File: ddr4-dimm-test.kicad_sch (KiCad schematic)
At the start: 1 part

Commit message: Update readme lol
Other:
- company: (none) -> WifiCable
- title: (none) -> Wifi-DDR4-UDIMM
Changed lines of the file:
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@@
 	(generator_version "8.0")
 	(paper "A2")
+	(title_block
+		(title "Wifi-DDR4-UDIMM")
+		(company "WifiCable")
+	)
 	(junction
 		(at 74.93 269.24)

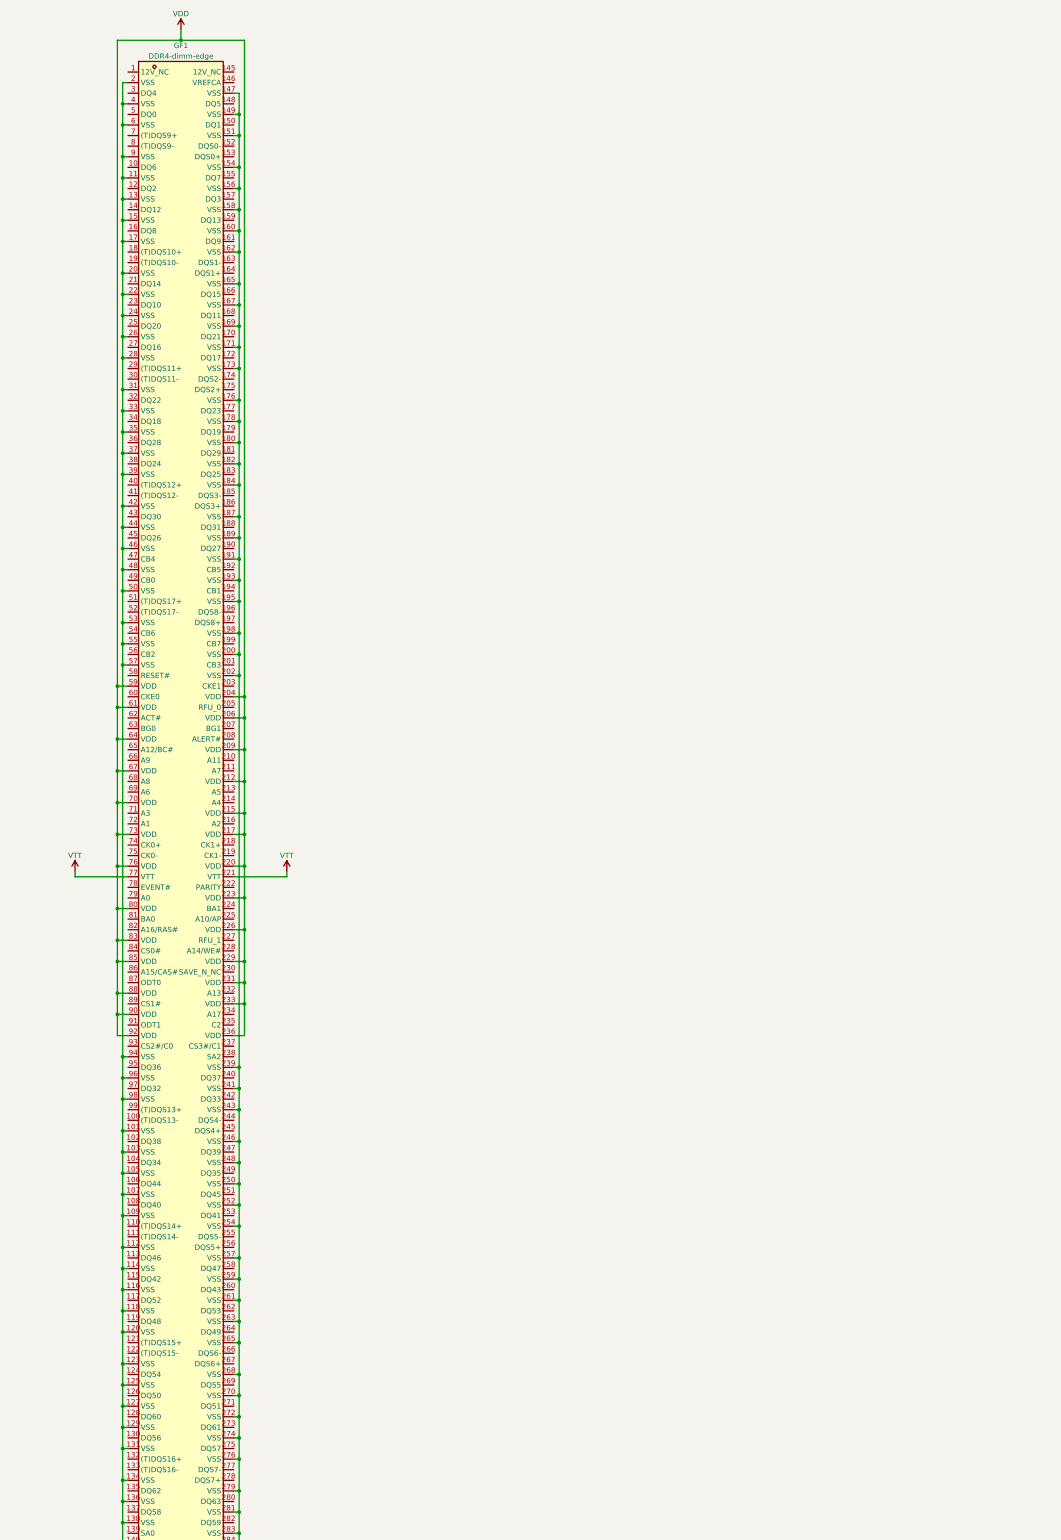
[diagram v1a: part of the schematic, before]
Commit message: Added ram chip symbol and partial connections
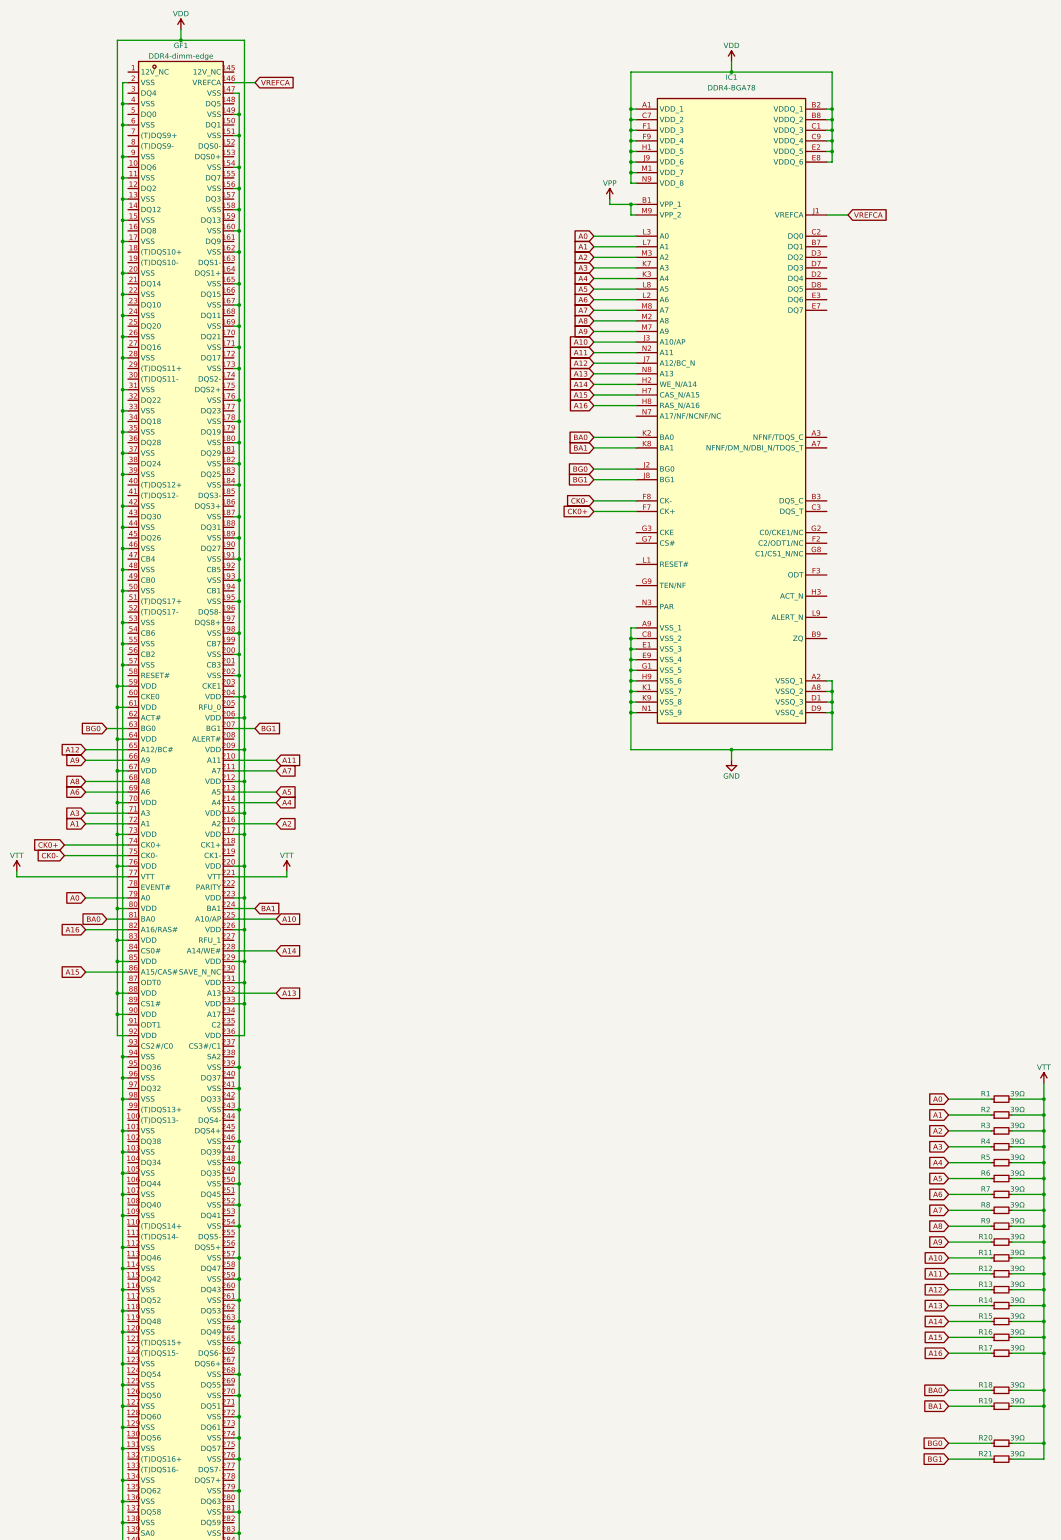
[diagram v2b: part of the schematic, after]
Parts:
- added IC1: DDR4-BGA78, A_my_stuff:DDR4-BGA78, symbol A_my_stuff:DDR4-BGA78
- added R1, R10, R11, R12, R13, R14, R15, R16, R17, R18, R19, R2, R20, R21, R3, R4, R5, R6, R7, R8, R9: 39Ω, Resistor_SMD:R_0402_1005Metric, symbol Device:R_Small
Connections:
- net GND: now also IC1.A2 (VSSQ_1), IC1.A8 (VSSQ_2), IC1.A9 (VSS_1), IC1.C8 (VSS_2), IC1.D1 (VSSQ_3), IC1.D9 (VSSQ_4), IC1.E1 (VSS_3), IC1.E9 (VSS_4), IC1.G1 (VSS_5), IC1.H9 (VSS_6), IC1.K1 (VSS_7), IC1.K9 (VSS_8), IC1.N1 (VSS_9)
- net VDD: now also IC1.A1 (VDD_1), IC1.B2 (VDDQ_1), IC1.B8 (VDDQ_2), IC1.C1 (VDDQ_3), IC1.C7 (VDD_2), IC1.C9 (VDDQ_4), IC1.E2 (VDDQ_5), IC1.E8 (VDDQ_6), IC1.F1 (VDD_3), IC1.F9 (VDD_4), IC1.H1 (VDD_5), IC1.J9 (VDD_6), IC1.M1 (VDD_7), IC1.N9 (VDD_8)
- net VPP: now also IC1.B1 (VPP_1), IC1.M9 (VPP_2)
- net VTT: now also R1.2, R10.2, R11.2, R12.2, R13.2, R14.2, R15.2, R16.2, R17.2, R18.2, R19.2, R2.2, R20.2, R21.2, R3.2, R4.2, R5.2, R6.2, R7.2, R8.2, R9.2
- net VREFCA: now reaches GF1.146 (VREFCA)
- net VREFCA: now also IC1.J1 (VREFCA)
- net BG1: now reaches GF1.207 (BG1)
- net BG1: now also IC1.J8 (BG1), R21.1
- net A11: now reaches GF1.210 (A11)
- net A11: now also IC1.N2 (A11), R12.1
- net A7: now reaches GF1.211 (A7)
- net A7: now also IC1.M8 (A7), R8.1
- net A5: now reaches GF1.213 (A5)
- net A5: now also IC1.L8 (A5), R6.1
- net A4: now reaches GF1.214 (A4)
- net A4: now also IC1.K3 (A4), R5.1
- net A2: now reaches GF1.216 (A2)
- net A2: now also IC1.M3 (A2), R3.1
- net BA1: now reaches GF1.224 (BA1)
- net BA1: now also IC1.K8 (BA1), R19.1
- net A10: now reaches GF1.225 (A10/AP)
- net A10: now also IC1.J3 (A10/AP), R11.1
- net A14: now reaches GF1.228 (A14/WE#)
- net A14: now also IC1.H2 (WE_N/A14), R15.1
- net A13: now reaches GF1.232 (A13)
- net A13: now also IC1.N8 (A13), R14.1
- net BG0: now reaches GF1.63 (BG0)
- net BG0: now also IC1.J2 (BG0), R20.1
- net A12: now reaches GF1.65 (A12/BC#)
- net A12: now also IC1.J7 (A12/BC_N), R13.1
- net A9: now reaches GF1.66 (A9)
- net A9: now also IC1.M7 (A9), R10.1
- net A8: now reaches GF1.68 (A8)
- net A8: now also IC1.M2 (A8), R9.1
- net A6: now reaches GF1.69 (A6)
- net A6: now also IC1.L2 (A6), R7.1
- net A3: now reaches GF1.71 (A3)
- net A3: now also IC1.K7 (A3), R4.1
- net A1: now reaches GF1.72 (A1)
- net A1: now also IC1.L7 (A1), R2.1
- net CK0+: now reaches GF1.74 (CK0+)
- net CK0+: now also IC1.F7 (CK+)
- net CK0-: now reaches GF1.75 (CK0-)
- net CK0-: now also IC1.F8 (CK-)
- net A0: now reaches GF1.79 (A0)
- net A0: now also IC1.L3 (A0), R1.1
- net BA0: now reaches GF1.81 (BA0)
- net BA0: now also IC1.K2 (BA0), R18.1
- net A16: now reaches GF1.82 (A16/RAS#)
- net A16: now also IC1.H8 (RAS_N/A16), R17.1
- net A15: now reaches GF1.86 (A15/CAS#)
- net A15: now also IC1.H7 (CAS_N/A15), R16.1

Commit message: Connected all common lines and duplicated chip
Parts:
- added C1: 0.01uF, Capacitor_SMD:C_0402_1005Metric, symbol Device:C_Small
- added C2: ?, Capacitor_SMD:C_0402_1005Metric, symbol Device:C_Small
- added C3: 10pF, Capacitor_SMD:C_0402_1005Metric, symbol Device:C_Small
- added IC2, IC3, IC4, IC5, IC6, IC7, IC8: DDR4-BGA78, A_my_stuff:DDR4-BGA78, symbol A_my_stuff:DDR4-BGA78
- added R22, R23, R24, R25, R26, R27, R28: 39Ω, Resistor_SMD:R_0402_1005Metric, symbol Device:R_Small
- added R29: 47Ω, Resistor_SMD:R_0402_1005Metric, symbol Device:R_Small
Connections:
- net A0: now also IC2.L3 (A0), IC3.L3 (A0), IC4.L3 (A0), IC5.L3 (A0), IC6.L3 (A0), IC7.L3 (A0), IC8.L3 (A0)
- net A1: now also IC2.L7 (A1), IC3.L7 (A1), IC4.L7 (A1), IC5.L7 (A1), IC6.L7 (A1), IC7.L7 (A1), IC8.L7 (A1)
- net A10: now also IC2.J3 (A10/AP), IC3.J3 (A10/AP), IC4.J3 (A10/AP), IC5.J3 (A10/AP), IC6.J3 (A10/AP), IC7.J3 (A10/AP), IC8.J3 (A10/AP)
- net A11: now also IC2.N2 (A11), IC3.N2 (A11), IC4.N2 (A11), IC5.N2 (A11), IC6.N2 (A11), IC7.N2 (A11), IC8.N2 (A11)
- net A12: now also IC2.J7 (A12/BC_N), IC3.J7 (A12/BC_N), IC4.J7 (A12/BC_N), IC5.J7 (A12/BC_N), IC6.J7 (A12/BC_N), IC7.J7 (A12/BC_N), IC8.J7 (A12/BC_N)
- net A13: now also IC2.N8 (A13), IC3.N8 (A13), IC4.N8 (A13), IC5.N8 (A13), IC6.N8 (A13), IC7.N8 (A13), IC8.N8 (A13)
- net A14: now also IC2.H2 (WE_N/A14), IC3.H2 (WE_N/A14), IC4.H2 (WE_N/A14), IC5.H2 (WE_N/A14), IC6.H2 (WE_N/A14), IC7.H2 (WE_N/A14), IC8.H2 (WE_N/A14)
- net A15: now also IC2.H7 (CAS_N/A15), IC3.H7 (CAS_N/A15), IC4.H7 (CAS_N/A15), IC5.H7 (CAS_N/A15), IC6.H7 (CAS_N/A15), IC7.H7 (CAS_N/A15), IC8.H7 (CAS_N/A15)
- net A16: now also IC2.H8 (RAS_N/A16), IC3.H8 (RAS_N/A16), IC4.H8 (RAS_N/A16), IC5.H8 (RAS_N/A16), IC6.H8 (RAS_N/A16), IC7.H8 (RAS_N/A16), IC8.H8 (RAS_N/A16)
- net A2: now also IC2.M3 (A2), IC3.M3 (A2), IC4.M3 (A2), IC5.M3 (A2), IC6.M3 (A2), IC7.M3 (A2), IC8.M3 (A2)
- net A3: now also IC2.K7 (A3), IC3.K7 (A3), IC4.K7 (A3), IC5.K7 (A3), IC6.K7 (A3), IC7.K7 (A3), IC8.K7 (A3)
- net A4: now also IC2.K3 (A4), IC3.K3 (A4), IC4.K3 (A4), IC5.K3 (A4), IC6.K3 (A4), IC7.K3 (A4), IC8.K3 (A4)
- net A5: now also IC2.L8 (A5), IC3.L8 (A5), IC4.L8 (A5), IC5.L8 (A5), IC6.L8 (A5), IC7.L8 (A5), IC8.L8 (A5)
- net A6: now also IC2.L2 (A6), IC3.L2 (A6), IC4.L2 (A6), IC5.L2 (A6), IC6.L2 (A6), IC7.L2 (A6), IC8.L2 (A6)
- net A7: now also IC2.M8 (A7), IC3.M8 (A7), IC4.M8 (A7), IC5.M8 (A7), IC6.M8 (A7), IC7.M8 (A7), IC8.M8 (A7)
- net A8: now also IC2.M2 (A8), IC3.M2 (A8), IC4.M2 (A8), IC5.M2 (A8), IC6.M2 (A8), IC7.M2 (A8), IC8.M2 (A8)
- net A9: now also IC2.M7 (A9), IC3.M7 (A9), IC4.M7 (A9), IC5.M7 (A9), IC6.M7 (A9), IC7.M7 (A9), IC8.M7 (A9)
- net BA0: now also IC2.K2 (BA0), IC3.K2 (BA0), IC4.K2 (BA0), IC5.K2 (BA0), IC6.K2 (BA0), IC7.K2 (BA0), IC8.K2 (BA0)
- net BA1: now also IC2.K8 (BA1), IC3.K8 (BA1), IC4.K8 (BA1), IC5.K8 (BA1), IC6.K8 (BA1), IC7.K8 (BA1), IC8.K8 (BA1)
- net BG0: now also IC2.J2 (BG0), IC3.J2 (BG0), IC4.J2 (BG0), IC5.J2 (BG0), IC6.J2 (BG0), IC7.J2 (BG0), IC8.J2 (BG0)
- net BG1: now also IC2.J8 (BG1), IC3.J8 (BG1), IC4.J8 (BG1), IC5.J8 (BG1), IC6.J8 (BG1), IC7.J8 (BG1), IC8.J8 (BG1)
- net CK0+: now also C2.1, IC2.F7 (CK+), IC3.F7 (CK+), IC4.F7 (CK+), IC5.F7 (CK+), IC6.F7 (CK+), IC7.F7 (CK+), IC8.F7 (CK+), R23.1
- net CK0-: now also C2.2, IC2.F8 (CK-), IC3.F8 (CK-), IC4.F8 (CK-), IC5.F8 (CK-), IC6.F8 (CK-), IC7.F8 (CK-), IC8.F8 (CK-), R22.1
- net GND: now also C3.2, IC2.A2 (VSSQ_1), IC2.A8 (VSSQ_2), IC2.A9 (VSS_1), IC2.C8 (VSS_2), IC2.D1 (VSSQ_3), IC2.D9 (VSSQ_4), IC2.E1 (VSS_3), IC2.E9 (VSS_4), IC2.G1 (VSS_5), IC2.H9 (VSS_6), IC2.K1 (VSS_7), IC2.K9 (VSS_8), IC2.N1 (VSS_9), IC3.A2 (VSSQ_1), IC3.A8 (VSSQ_2), IC3.A9 (VSS_1), IC3.C8 (VSS_2), IC3.D1 (VSSQ_3), IC3.D9 (VSSQ_4), IC3.E1 (VSS_3), IC3.E9 (VSS_4), IC3.G1 (VSS_5), IC3.H9 (VSS_6), IC3.K1 (VSS_7), IC3.K9 (VSS_8), IC3.N1 (VSS_9), IC4.A2 (VSSQ_1), IC4.A8 (VSSQ_2), IC4.A9 (VSS_1), IC4.C8 (VSS_2), IC4.D1 (VSSQ_3), IC4.D9 (VSSQ_4), IC4.E1 (VSS_3), IC4.E9 (VSS_4), IC4.G1 (VSS_5), IC4.H9 (VSS_6), IC4.K1 (VSS_7), IC4.K9 (VSS_8), IC4.N1 (VSS_9), IC5.A2 (VSSQ_1), IC5.A8 (VSSQ_2), IC5.A9 (VSS_1), IC5.C8 (VSS_2), IC5.D1 (VSSQ_3), IC5.D9 (VSSQ_4), IC5.E1 (VSS_3), IC5.E9 (VSS_4), IC5.G1 (VSS_5), IC5.H9 (VSS_6), IC5.K1 (VSS_7), IC5.K9 (VSS_8), IC5.N1 (VSS_9), IC6.A2 (VSSQ_1), IC6.A8 (VSSQ_2), IC6.A9 (VSS_1), IC6.C8 (VSS_2), IC6.D1 (VSSQ_3), IC6.D9 (VSSQ_4), IC6.E1 (VSS_3), IC6.E9 (VSS_4), IC6.G1 (VSS_5), IC6.H9 (VSS_6), IC6.K1 (VSS_7), IC6.K9 (VSS_8), IC6.N1 (VSS_9), IC7.A2 (VSSQ_1), IC7.A8 (VSSQ_2), IC7.A9 (VSS_1), IC7.C8 (VSS_2), IC7.D1 (VSSQ_3), IC7.D9 (VSSQ_4), IC7.E1 (VSS_3), IC7.E9 (VSS_4), IC7.G1 (VSS_5), IC7.H9 (VSS_6), IC7.K1 (VSS_7), IC7.K9 (VSS_8), IC7.N1 (VSS_9), IC8.A2 (VSSQ_1), IC8.A8 (VSSQ_2), IC8.A9 (VSS_1), IC8.C8 (VSS_2), IC8.D1 (VSSQ_3), IC8.D9 (VSSQ_4), IC8.E1 (VSS_3), IC8.E9 (VSS_4), IC8.G1 (VSS_5), IC8.H9 (VSS_6), IC8.K1 (VSS_7), IC8.K9 (VSS_8), IC8.N1 (VSS_9)
- net VDD: now also C1.2, IC2.A1 (VDD_1), IC2.B2 (VDDQ_1), IC2.B8 (VDDQ_2), IC2.C1 (VDDQ_3), IC2.C7 (VDD_2), IC2.C9 (VDDQ_4), IC2.E2 (VDDQ_5), IC2.E8 (VDDQ_6), IC2.F1 (VDD_3), IC2.F9 (VDD_4), IC2.H1 (VDD_5), IC2.J9 (VDD_6), IC2.M1 (VDD_7), IC2.N9 (VDD_8), IC3.A1 (VDD_1), IC3.B2 (VDDQ_1), IC3.B8 (VDDQ_2), IC3.C1 (VDDQ_3), IC3.C7 (VDD_2), IC3.C9 (VDDQ_4), IC3.E2 (VDDQ_5), IC3.E8 (VDDQ_6), IC3.F1 (VDD_3), IC3.F9 (VDD_4), IC3.H1 (VDD_5), IC3.J9 (VDD_6), IC3.M1 (VDD_7), IC3.N9 (VDD_8), IC4.A1 (VDD_1), IC4.B2 (VDDQ_1), IC4.B8 (VDDQ_2), IC4.C1 (VDDQ_3), IC4.C7 (VDD_2), IC4.C9 (VDDQ_4), IC4.E2 (VDDQ_5), IC4.E8 (VDDQ_6), IC4.F1 (VDD_3), IC4.F9 (VDD_4), IC4.H1 (VDD_5), IC4.J9 (VDD_6), IC4.M1 (VDD_7), IC4.N9 (VDD_8), IC5.A1 (VDD_1), IC5.B2 (VDDQ_1), IC5.B8 (VDDQ_2), IC5.C1 (VDDQ_3), IC5.C7 (VDD_2), IC5.C9 (VDDQ_4), IC5.E2 (VDDQ_5), IC5.E8 (VDDQ_6), IC5.F1 (VDD_3), IC5.F9 (VDD_4), IC5.H1 (VDD_5), IC5.J9 (VDD_6), IC5.M1 (VDD_7), IC5.N9 (VDD_8), IC6.A1 (VDD_1), IC6.B2 (VDDQ_1), IC6.B8 (VDDQ_2), IC6.C1 (VDDQ_3), IC6.C7 (VDD_2), IC6.C9 (VDDQ_4), IC6.E2 (VDDQ_5), IC6.E8 (VDDQ_6), IC6.F1 (VDD_3), IC6.F9 (VDD_4), IC6.H1 (VDD_5), IC6.J9 (VDD_6), IC6.M1 (VDD_7), IC6.N9 (VDD_8), IC7.A1 (VDD_1), IC7.B2 (VDDQ_1), IC7.B8 (VDDQ_2), IC7.C1 (VDDQ_3), IC7.C7 (VDD_2), IC7.C9 (VDDQ_4), IC7.E2 (VDDQ_5), IC7.E8 (VDDQ_6), IC7.F1 (VDD_3), IC7.F9 (VDD_4), IC7.H1 (VDD_5), IC7.J9 (VDD_6), IC7.M1 (VDD_7), IC7.N9 (VDD_8), IC8.A1 (VDD_1), IC8.B2 (VDDQ_1), IC8.B8 (VDDQ_2), IC8.C1 (VDDQ_3), IC8.C7 (VDD_2), IC8.C9 (VDDQ_4), IC8.E2 (VDDQ_5), IC8.E8 (VDDQ_6), IC8.F1 (VDD_3), IC8.F9 (VDD_4), IC8.H1 (VDD_5), IC8.J9 (VDD_6), IC8.M1 (VDD_7), IC8.N9 (VDD_8), R29.2
- net VPP: now also IC2.B1 (VPP_1), IC2.M9 (VPP_2), IC3.B1 (VPP_1), IC3.M9 (VPP_2), IC4.B1 (VPP_1), IC4.M9 (VPP_2), IC5.B1 (VPP_1), IC5.M9 (VPP_2), IC6.B1 (VPP_1), IC6.M9 (VPP_2), IC7.B1 (VPP_1), IC7.M9 (VPP_2), IC8.B1 (VPP_1), IC8.M9 (VPP_2)
- net VREFCA: now also IC2.J1 (VREFCA), IC3.J1 (VREFCA), IC4.J1 (VREFCA), IC5.J1 (VREFCA), IC6.J1 (VREFCA), IC7.J1 (VREFCA), IC8.J1 (VREFCA)
- net VTT: now also R24.2, R25.2, R26.2, R27.2, R28.2
- net ODT0: now reaches IC1.F3 (ODT)
- net ODT0: now also GF1.87 (ODT0), IC2.F3 (ODT), IC3.F3 (ODT), IC4.F3 (ODT), IC5.F3 (ODT), IC6.F3 (ODT), IC7.F3 (ODT), IC8.F3 (ODT), R27.1
- net CKE0: now reaches IC1.G3 (CKE)
- net CKE0: now also GF1.60 (CKE0), IC2.G3 (CKE), IC3.G3 (CKE), IC4.G3 (CKE), IC5.G3 (CKE), IC6.G3 (CKE), IC7.G3 (CKE), IC8.G3 (CKE), R24.1
- net CS0#: now reaches IC1.G7 (CS#)
- net CS0#: now also GF1.84 (CS0#), IC2.G7 (CS#), IC3.G7 (CS#), IC4.G7 (CS#), IC5.G7 (CS#), IC6.G7 (CS#), IC7.G7 (CS#), IC8.G7 (CS#), R25.1
- net ACT#: now reaches IC1.H3 (ACT#)
- net ACT#: now also GF1.62 (ACT#), IC2.H3 (ACT#), IC3.H3 (ACT#), IC4.H3 (ACT#), IC5.H3 (ACT#), IC6.H3 (ACT#), IC7.H3 (ACT#), IC8.H3 (ACT#), R28.1
- net RESET#: now reaches IC1.L1 (RESET#)
- net RESET#: now also GF1.58 (RESET#), IC2.L1 (RESET#), IC3.L1 (RESET#), IC4.L1 (RESET#), IC5.L1 (RESET#), IC6.L1 (RESET#), IC7.L1 (RESET#), IC8.L1 (RESET#)
- net ALERT#: now reaches IC1.L9 (ALERT#)
- net ALERT#: now also GF1.208 (ALERT#), C3.1, IC2.L9 (ALERT#), IC3.L9 (ALERT#), IC4.L9 (ALERT#), IC5.L9 (ALERT#), IC6.L9 (ALERT#), IC7.L9 (ALERT#), IC8.L9 (ALERT#), R29.1
- net PARITY: now reaches IC1.N3 (PAR)
- net PARITY: now also GF1.222 (PARITY), IC2.N3 (PAR), IC3.N3 (PAR), IC4.N3 (PAR), IC5.N3 (PAR), IC6.N3 (PAR), IC7.N3 (PAR), IC8.N3 (PAR), R26.1
- new net: C1.1, R22.2, R23.2
- no-connect marks 0 -> 24
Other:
- moved on the sheet: GF1, IC1, R1, R10, R11, R12, R13, R14, R15, R16, R17, R18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

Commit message: Connected data bus
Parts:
- added R100, R101, R102, R103, R104, R105, R106, R107, R108, R109, R110, R111, R112, R113, R114, R115, R116, R117, R118, R119, R120, R121, R122, R123, R124, R125, R38, R39, R40, R41, R42, R43, R44, R45, R46, R47, R48, R49, R50, R51, R52, R53, R54, R55, R56, R57, R58, R59, R60, R61, R62, R63, R64, R65, R66, R67, R68, R69, R70, R71, R72, R73, R74, R75, R76, R77, R78, R79, R80, R81, R82, R83, R84, R85, R86, R87, R88, R89, R90, R91, R92, R93, R94, R95, R96, R97, R98, R99: 15Ω, Resistor_SMD:R_0402_1005Metric, symbol Device:R_Small
- added R30, R31, R32, R33, R34, R35, R36, R37: 240Ω, Resistor_SMD:R_0402_1005Metric, symbol Device:R_Small
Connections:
- net GND: now also R30.2, R31.2, R32.2, R33.2, R34.2, R35.2, R36.2, R37.2
- net DM6: now reaches IC7.A7 (NFNF/DM_N/DBI_N/TDQS_T)
- net DM6: now also R61.1
- net DQS6-: now reaches IC7.B3 (DQS_C)
- net DQS6-: now also R50.2
- net DQ49: now reaches IC7.B7 (DQ1)
- net DQ49: now also R87.2
- net at IC7.B9 (ZQ): now also R36.1
- net DQ48: now reaches IC7.C2 (DQ0)
- net DQ48: now also R119.1
- net DQS6+: now reaches IC7.C3 (DQS_T)
- net DQS6+: now also R51.2
- net DQ52: now reaches IC7.D2 (DQ4)
- net DQ52: now also R118.1
- net DQ50: now reaches IC7.D3 (DQ2)
- net DQ50: now also R121.1
- net DQ51: now reaches IC7.D7 (DQ3)
- net DQ51: now also R89.2
- net DQ53: now reaches IC7.D8 (DQ5)
- net DQ53: now also R86.2
- net DQ54: now reaches IC7.E3 (DQ6)
- net DQ54: now also R120.1
- net DQ55: now reaches IC7.E7 (DQ7)
- net DQ55: now also R88.2
- net DM4: now reaches IC5.A7 (NFNF/DM_N/DBI_N/TDQS_T)
- net DM4: now also R59.1
- net DQS4-: now reaches IC5.B3 (DQS_C)
- net DQS4-: now also R46.2
- net DQ33: now reaches IC5.B7 (DQ1)
- net DQ33: now also R79.2
- net at IC5.B9 (ZQ): now also R34.1
- net DQ32: now reaches IC5.C2 (DQ0)
- net DQ32: now also R111.1
- net DQS4+: now reaches IC5.C3 (DQS_T)
- net DQS4+: now also R47.2
- net DQ36: now reaches IC5.D2 (DQ4)
- net DQ36: now also R110.1
- net DQ34: now reaches IC5.D3 (DQ2)
- net DQ34: now also R113.1
- net DQ35: now reaches IC5.D7 (DQ3)
- net DQ35: now also R81.2
- net DQ37: now reaches IC5.D8 (DQ5)
- net DQ37: now also R78.2
- net DQ38: now reaches IC5.E3 (DQ6)
- net DQ38: now also R112.1
- net DQ39: now reaches IC5.E7 (DQ7)
- net DQ39: now also R80.2
- net DM5: now reaches IC6.A7 (NFNF/DM_N/DBI_N/TDQS_T)
- net DM5: now also R60.1
- net DQS5-: now reaches IC6.B3 (DQS_C)
- net DQS5-: now also R48.2
- net DQ41: now reaches IC6.B7 (DQ1)
- net DQ41: now also R83.2
- net at IC6.B9 (ZQ): now also R35.1
- net DQ40: now reaches IC6.C2 (DQ0)
- net DQ40: now also R115.1
- net DQS5+: now reaches IC6.C3 (DQS_T)
- net DQS5+: now also R49.2
- net DQ44: now reaches IC6.D2 (DQ4)
- net DQ44: now also R114.1
- net DQ42: now reaches IC6.D3 (DQ2)
- net DQ42: now also R117.1
- net DQ43: now reaches IC6.D7 (DQ3)
- net DQ43: now also R85.2
- net DQ45: now reaches IC6.D8 (DQ5)
- net DQ45: now also R82.2
- net DQ46: now reaches IC6.E3 (DQ6)
- net DQ46: now also R116.1
- net DQ47: now reaches IC6.E7 (DQ7)
- net DQ47: now also R84.2
- net DM7: now reaches IC8.A7 (NFNF/DM_N/DBI_N/TDQS_T)
- net DM7: now also R62.1
- net DQS7-: now reaches IC8.B3 (DQS_C)
- net DQS7-: now also R52.2
- net DQ57: now reaches IC8.B7 (DQ1)
- net DQ57: now also R91.2
- net at IC8.B9 (ZQ): now also R37.1
- net DQ56: now reaches IC8.C2 (DQ0)
- net DQ56: now also R123.1
- net DQS7+: now reaches IC8.C3 (DQS_T)
- net DQS7+: now also R53.2
- net DQ60: now reaches IC8.D2 (DQ4)
- net DQ60: now also R122.1
- net DQ58: now reaches IC8.D3 (DQ2)
- net DQ58: now also R125.1
- net DQ59: now reaches IC8.D7 (DQ3)
- net DQ59: now also R93.2
- net DQ61: now reaches IC8.D8 (DQ5)
- net DQ61: now also R90.2
- net DQ62: now reaches IC8.E3 (DQ6)
- net DQ62: now also R124.1
- net DQ63: now reaches IC8.E7 (DQ7)
- net DQ63: now also R92.2
- net DM0: now reaches IC1.A7 (NFNF/DM_N/DBI_N/TDQS_T)
- net DM0: now also R54.1
- net DQS0-: now reaches IC1.B3 (DQS_C)
- net DQS0-: now also R38.2
- net DQ1: now reaches IC1.B7 (DQ1)
- net DQ1: now also R63.2
- net at IC1.B9 (ZQ): now also R30.1
- net DQ0: now reaches IC1.C2 (DQ0)
- net DQ0: now also R95.1
- net DQS0+: now reaches IC1.C3 (DQS_T)
- net DQS0+: now also R39.2
- net DQ4: now reaches IC1.D2 (DQ4)
- net DQ4: now also R94.1
- net DQ2: now reaches IC1.D3 (DQ2)
- net DQ2: now also R97.1
- net DQ3: now reaches IC1.D7 (DQ3)
- net DQ3: now also R65.2
- net DQ5: now reaches IC1.D8 (DQ5)
- net DQ5: now also R58.2
- net DQ6: now reaches IC1.E3 (DQ6)
- net DQ6: now also R96.1
- net DQ7: now reaches IC1.E7 (DQ7)
- net DQ7: now also R64.2
- net DM2: now reaches IC3.A7 (NFNF/DM_N/DBI_N/TDQS_T)
- net DM2: now also R56.1
- net DQS2-: now reaches IC3.B3 (DQS_C)
- net DQS2-: now also R42.2
- net DQ17: now reaches IC3.B7 (DQ1)
- net DQ17: now also R71.2
- net at IC3.B9 (ZQ): now also R32.1
- net DQ16: now reaches IC3.C2 (DQ0)
- net DQ16: now also R103.1
- net DQS2+: now reaches IC3.C3 (DQS_T)
- net DQS2+: now also R43.2
- net DQ20: now reaches IC3.D2 (DQ4)
- net DQ20: now also R102.1
- net DQ18: now reaches IC3.D3 (DQ2)
- net DQ18: now also R105.1
- net DQ19: now reaches IC3.D7 (DQ3)
- net DQ19: now also R73.2
- net DQ21: now reaches IC3.D8 (DQ5)
- net DQ21: now also R70.2
- net DQ22: now reaches IC3.E3 (DQ6)
- net DQ22: now also R104.1
- net DQ23: now reaches IC3.E7 (DQ7)
- net DQ23: now also R72.2
- net DM1: now reaches IC2.A7 (NFNF/DM_N/DBI_N/TDQS_T)
- net DM1: now also R55.1
- net DQS1-: now reaches IC2.B3 (DQS_C)
- net DQS1-: now also R40.2
- net DQ9: now reaches IC2.B7 (DQ1)
- net DQ9: now also R67.2
- net at IC2.B9 (ZQ): now also R31.1
- net DQ8: now reaches IC2.C2 (DQ0)
- net DQ8: now also R99.1
- net DQS1+: now reaches IC2.C3 (DQS_T)
- net DQS1+: now also R41.2
- net DQ12: now reaches IC2.D2 (DQ4)
- net DQ12: now also R98.1
- net DQ10: now reaches IC2.D3 (DQ2)
- net DQ10: now also R101.1
- net DQ11: now reaches IC2.D7 (DQ3)
- net DQ11: now also R69.2
- net DQ13: now reaches IC2.D8 (DQ5)
- net DQ13: now also R66.2
- net DQ14: now reaches IC2.E3 (DQ6)
- net DQ14: now also R100.1
- net DQ15: now reaches IC2.E7 (DQ7)
- net DQ15: now also R68.2
- net DM3: now reaches IC4.A7 (NFNF/DM_N/DBI_N/TDQS_T)
- net DM3: now also R57.1
- net DQS3-: now reaches IC4.B3 (DQS_C)
- net DQS3-: now also R44.2
- net DQ25: now reaches IC4.B7 (DQ1)
- net DQ25: now also R75.2
- net at IC4.B9 (ZQ): now also R33.1
- net DQ24: now reaches IC4.C2 (DQ0)
- net DQ24: now also R107.1
- net DQS3+: now reaches IC4.C3 (DQS_T)
- net DQS3+: now also R45.2
- net DQ28: now reaches IC4.D2 (DQ4)
- net DQ28: now also R106.1
- net DQ26: now reaches IC4.D3 (DQ2)
- net DQ26: now also R109.1
- net DQ27: now reaches IC4.D7 (DQ3)
- net DQ27: now also R77.2
- net DQ29: now reaches IC4.D8 (DQ5)
- net DQ29: now also R74.2
- net DQ30: now reaches IC4.E3 (DQ6)
- net DQ30: now also R108.1
- net DQ31: now reaches IC4.E7 (DQ7)
- net DQ31: now also R76.2
- net at GF1.10 (DQ6): now also R96.2
- net at GF1.102 (DQ38): now also R112.2
- net at GF1.104 (DQ34): now also R113.2
- net at GF1.106 (DQ44): now also R114.2
- net at GF1.108 (DQ40): now also R115.2
- net R_DM5: now reaches GF1.110 ((T)DQS14+)
- net R_DM5: now also R60.2
- net at GF1.113 (DQ46): now also R116.2
- net at GF1.115 (DQ42): now also R117.2
- net at GF1.117 (DQ52): now also R118.2
- net at GF1.119 (DQ48): now also R119.2
- net at GF1.12 (DQ2): now also R97.2
- net R_DM6: now reaches GF1.121 ((T)DQS15+)
- net R_DM6: now also R61.2
- net at GF1.124 (DQ54): now also R120.2
- net at GF1.126 (DQ50): now also R121.2
- net at GF1.128 (DQ60): now also R122.2
- net at GF1.130 (DQ56): now also R123.2
- net R_DM7: now reaches GF1.132 ((T)DQS16+)
- net R_DM7: now also R62.2
- net at GF1.135 (DQ62): now also R124.2
- net at GF1.137 (DQ58): now also R125.2
- net at GF1.14 (DQ12): now also R98.2
- net at GF1.148 (DQ5): now also R58.1
- net at GF1.150 (DQ1): now also R63.1
- net R_DQS0-: now reaches GF1.152 (DQS0-)
- net R_DQS0-: now also R38.1
- net R_DQS0+: now reaches GF1.153 (DQS0+)
- net R_DQS0+: now also R39.1
- net at GF1.155 (DQ7): now also R64.1
- net at GF1.157 (DQ3): now also R65.1
- net at GF1.159 (DQ13): now also R66.1
- net at GF1.16 (DQ8): now also R99.2
- net at GF1.161 (DQ9): now also R67.1
- net R_DQS1-: now reaches GF1.163 (DQS1-)
- net R_DQS1-: now also R40.1
- net R_DQS1+: now reaches GF1.164 (DQS1+)
- net R_DQS1+: now also R41.1
- net at GF1.166 (DQ15): now also R68.1
- net at GF1.168 (DQ11): now also R69.1
- net at GF1.170 (DQ21): now also R70.1
- net at GF1.172 (DQ17): now also R71.1
- net R_DQS2-: now reaches GF1.174 (DQS2-)
- net R_DQS2-: now also R42.1
- net R_DQS2+: now reaches GF1.175 (DQS2+)
- net R_DQS2+: now also R43.1
- net at GF1.177 (DQ23): now also R72.1
- net at GF1.179 (DQ19): now also R73.1
- net R_DM1: now reaches GF1.18 ((T)DQS10+)
- net R_DM1: now also R55.2
- net at GF1.181 (DQ29): now also R74.1
- net at GF1.183 (DQ25): now also R75.1
- net R_DQS3-: now reaches GF1.185 (DQS3-)
- net R_DQS3-: now also R44.1
- net R_DQS3+: now reaches GF1.186 (DQS3+)
- net R_DQS3+: now also R45.1
- net at GF1.188 (DQ31): now also R76.1
- net at GF1.190 (DQ27): now also R77.1
- net at GF1.21 (DQ14): now also R100.2
- net at GF1.23 (DQ10): now also R101.2
- net at GF1.240 (DQ37): now also R78.1
- net at GF1.242 (DQ33): now also R79.1
- net R_DQS4-: now reaches GF1.244 (DQS4-)
- net R_DQS4-: now also R46.1
- net R_DQS4+: now reaches GF1.245 (DQS4+)
- net R_DQS4+: now also R47.1
- net at GF1.247 (DQ39): now also R80.1
- net at GF1.249 (DQ35): now also R81.1
- net at GF1.25 (DQ20): now also R102.2
- net at GF1.251 (DQ45): now also R82.1
- net at GF1.253 (DQ41): now also R83.1
- net R_DQS5-: now reaches GF1.255 (DQS5-)
- net R_DQS5-: now also R48.1
- net R_DQS5+: now reaches GF1.256 (DQS5+)
- net R_DQS5+: now also R49.1
- net at GF1.258 (DQ47): now also R84.1
- net at GF1.260 (DQ43): now also R85.1
- net at GF1.262 (DQ53): now also R86.1
- net at GF1.264 (DQ49): now also R87.1
- net R_DQS6-: now reaches GF1.266 (DQS6-)
- net R_DQS6-: now also R50.1
- net R_DQS6+: now reaches GF1.267 (DQS6+)
- net R_DQS6+: now also R51.1
- net at GF1.269 (DQ55): now also R88.1
- net at GF1.27 (DQ16): now also R103.2
- net at GF1.271 (DQ51): now also R89.1
- net at GF1.273 (DQ61): now also R90.1
- net at GF1.275 (DQ57): now also R91.1
- net R_DQS7-: now reaches GF1.277 (DQS7-)
- net R_DQS7-: now also R52.1
- net R_DQS7+: now reaches GF1.278 (DQS7+)
- net R_DQS7+: now also R53.1
- net at GF1.280 (DQ63): now also R92.1
- net at GF1.282 (DQ59): now also R93.1
- net R_DM2: now reaches GF1.29 ((T)DQS11+)
- net R_DM2: now also R56.2
- net at GF1.3 (DQ4): now also R94.2
- net at GF1.32 (DQ22): now also R104.2
- net at GF1.34 (DQ18): now also R105.2
- net at GF1.36 (DQ28): now also R106.2
- net at GF1.38 (DQ24): now also R107.2
- net R_DM3: now reaches GF1.40 ((T)DQS12+)
- net R_DM3: now also R57.2
- net at GF1.43 (DQ30): now also R108.2
- net at GF1.45 (DQ26): now also R109.2
- net at GF1.5 (DQ0): now also R95.2
- net R_DM0: now reaches GF1.7 ((T)DQS9+)
- net R_DM0: now also R54.2
- net at GF1.95 (DQ36): now also R110.2
- net at GF1.97 (DQ32): now also R111.2
- net R_DM4: now reaches GF1.99 ((T)DQS13+)
- net R_DM4: now also R59.2
- no-connect marks 24 -> 40

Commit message: Some more layout testing
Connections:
- net DQ0: now also IC1.D7 (DQ3); no longer IC1.C2 (DQ0)
- net DQ1: now also IC1.E7 (DQ7); no longer IC1.B7 (DQ1)
- net DQ3: now also IC1.C2 (DQ0); no longer IC1.D7 (DQ3)
- net DQ4: now also IC1.B7 (DQ1); no longer IC1.D2 (DQ4)
- net DQ7: now also IC1.D2 (DQ4); no longer IC1.E7 (DQ7)
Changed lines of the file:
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@@
 	(global_label "DQ3"
 		(shape input)
-		(at 205.74 74.93 0)
+		(at 205.74 67.31 0)
 		(fields_autoplaced yes)
 		(effects
@@
 		)
 		(property "Intersheetrefs" "${INTERSHEET_REFS}"
-			(at 214.0471 74.93 0)
+			(at 214.0471 67.31 0)
 			(effects
 				(font
@@
 	(global_label "DQ1"
 		(shape input)
-		(at 205.74 69.85 0)
+		(at 205.74 85.09 0)
 		(fields_autoplaced yes)
 		(effects
@@
 		)
 		(property "Intersheetrefs" "${INTERSHEET_REFS}"
-			(at 214.0471 69.85 0)
+			(at 214.0471 85.09 0)
 			(effects
 				(font
@@
 	(global_label "DQ4"
 		(shape input)
-		(at 205.74 77.47 0)
+		(at 205.74 69.85 0)
 		(fields_autoplaced yes)
 		(effects
@@
 		)
 		(property "Intersheetrefs" "${INTERSHEET_REFS}"
-			(at 214.0471 77.47 0)
+			(at 214.0471 69.85 0)
 			(effects
 				(font
@@
 	(global_label "DQ7"
 		(shape input)
-		(at 205.74 85.09 0)
+		(at 205.74 77.47 0)
 		(fields_autoplaced yes)
 		(effects
@@
 		)
 		(property "Intersheetrefs" "${INTERSHEET_REFS}"
-			(at 214.0471 85.09 0)
+			(at 214.0471 77.47 0)
 			(effects
 				(font
@@
 	(global_label "DQ0"
 		(shape input)
-		(at 205.74 67.31 0)
+		(at 205.74 74.93 0)
 		(fields_autoplaced yes)
 		(effects
@@
 		)
 		(property "Intersheetrefs" "${INTERSHEET_REFS}"
-			(at 214.0471 67.31 0)
+			(at 214.0471 74.93 0)
 			(effects
 				(font
